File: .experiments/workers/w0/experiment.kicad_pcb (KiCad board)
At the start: 2 copper layers, 140 x 90 mm, 39 parts, among them J1 USB_C, J2 Output, J3 Debug, Q1 FS8205A, U1 USBLC6-2SC6, U2 BQ24072, U3 HY2113-KB5B, U4 MT3608, U5 AP2112K-3.3, U6 LN61CN3302MR-G

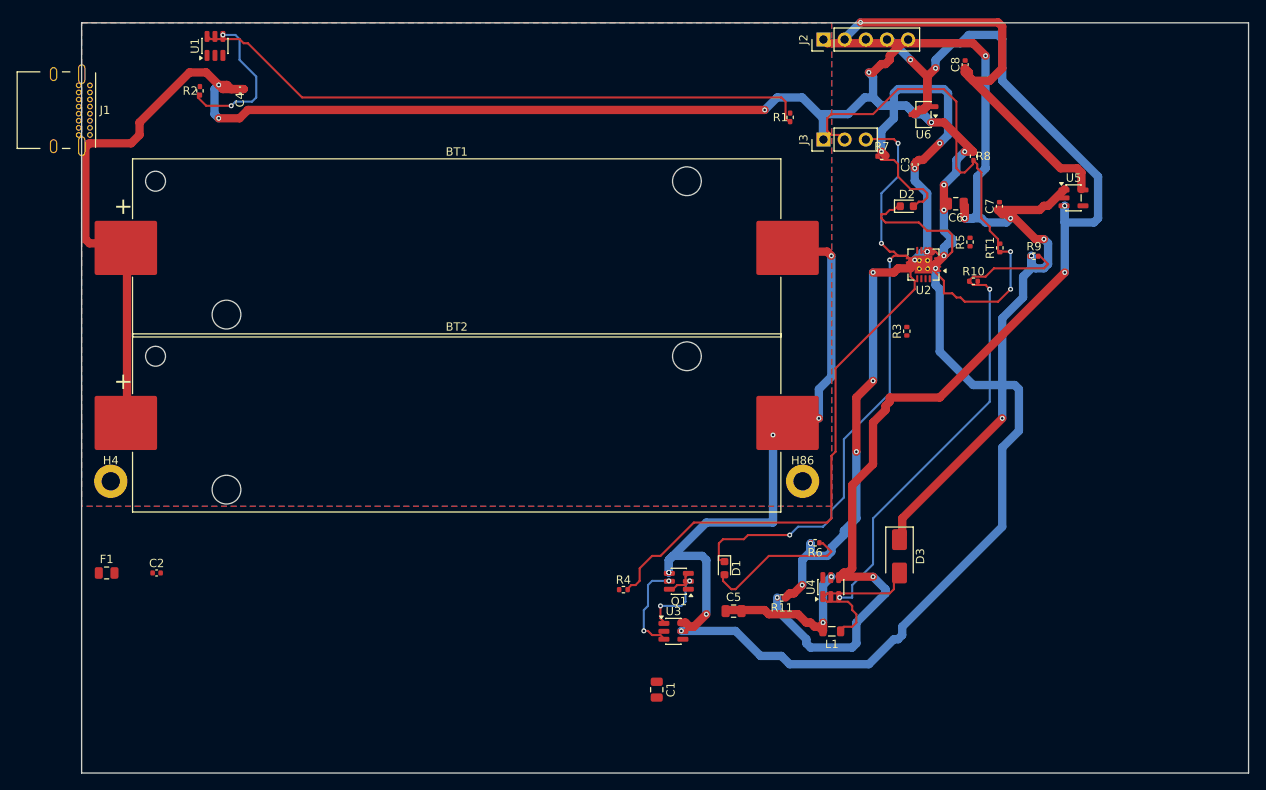
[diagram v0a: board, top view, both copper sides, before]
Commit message: 35-round experiment: best score 25.33, improved routing params
Router and conflict resolution tuning from autonomous optimization loop.
Best config: clearance=0.2051mm, cooling_factor=0.9735, existing_trace_cost=200.0

Co-Authored-By: Claude Opus 4.6 <noreply@anthropic.com>
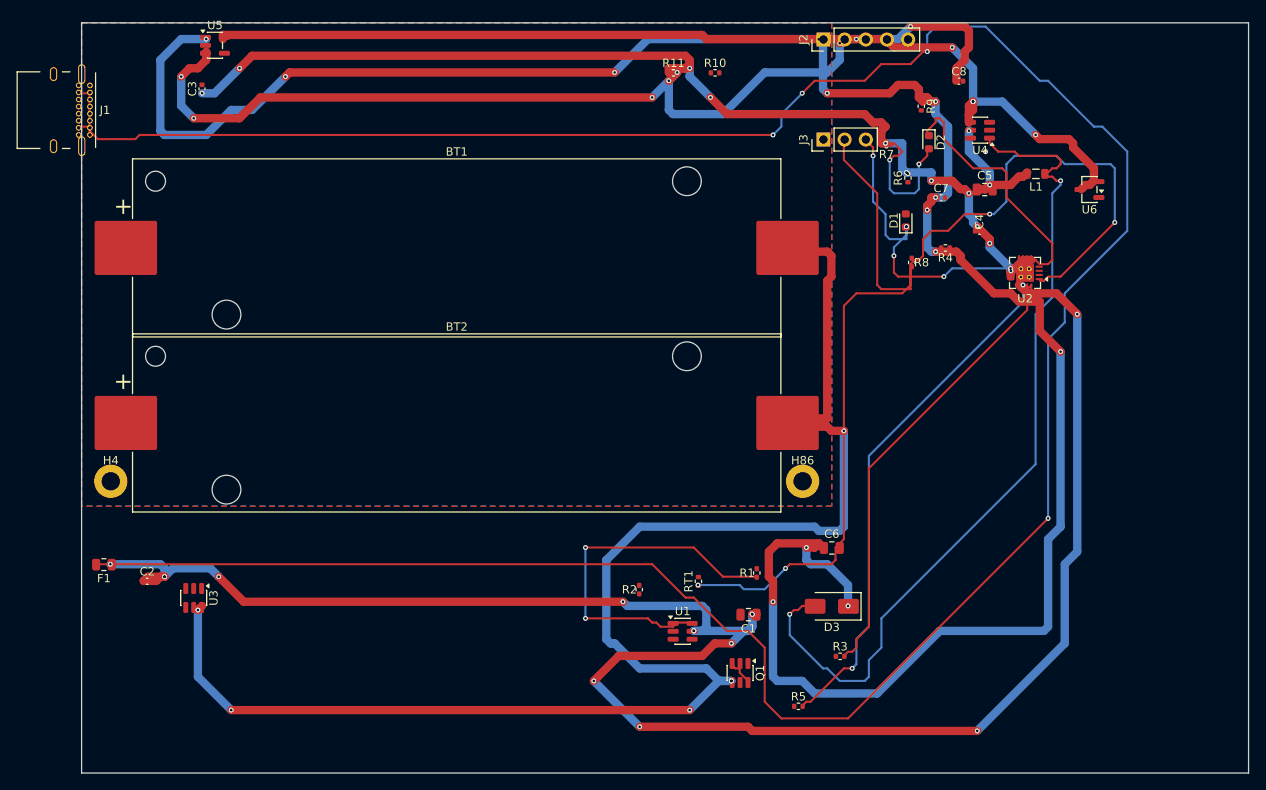
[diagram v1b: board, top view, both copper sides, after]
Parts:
- moved U5 104.6 mm to (16.0, 2.69)
- moved C4 90.3 mm to (107.7, 25.0), turned to 0 degrees
- moved U1 89.9 mm to (72.1, 73.0), turned to 0 degrees
- moved C3 86.0 mm to (14.4, 7.91)
- moved R2 79.7 mm to (66.9, 68.0)
- moved R11 64.3 mm to (71.0, 6.00), turned to 0 degrees
- moved L1 60.1 mm to (114.5, 18.1)
- moved R5 59.4 mm to (86.0, 82.0), turned to 0 degrees
- moved C5 58.9 mm to (108.3, 20.0)
- moved U3 57.7 mm to (13.4, 69.0), turned to -90 degrees
- moved U4 57.7 mm to (107.8, 12.9), turned to 180 degrees
- moved R4 56.3 mm to (103.6, 27.0), turned to 180 degrees
- moved R1 54.8 mm to (81.0, 66.0)
- moved RT1 53.9 mm to (74.0, 67.0)
- moved D1 47.0 mm to (98.9, 23.7), turned to 90 degrees
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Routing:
- net Net-(F1-Pad2): track 0.00 -> 328.6 mm, vias 0 -> 4
- net /VBAT: track 293.0 -> 0.00 mm, vias 14 -> 0
- net /VBUS: track 0.00 -> 229.1 mm, vias 0 -> 14
- net /5V: track 115.5 -> 271.1 mm, vias 8 -> 14
- net /CELL_NEG: track 75.5 -> 182.7 mm
- net Net-(D3-A): track 19.7 -> 102.1 mm, vias 0 -> 2
- net /NTC_SENSE: track 62.8 -> 139.2 mm, vias 2 -> 4
- net Net-(U2-ILIM): track 62.7 -> 0.00 mm, vias 0 -> 1
- net Net-(U2-TMR): track 0.00 -> 62.4 mm, vias 0 -> 2
- net Net-(U4-FB): track 60.0 -> 0.00 mm, vias 2 -> 0
- net Net-(U2-ISET): track 0.00 -> 54.1 mm
- net /3V3: track 52.5 -> 97.7 mm
- net /CHG_N: track 75.4 -> 37.5 mm, vias 4 -> 6
- net /VSYS: track 93.0 -> 126.7 mm
- net Net-(R1-Pad1): track 75.5 -> 44.1 mm, vias 0 -> 2
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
